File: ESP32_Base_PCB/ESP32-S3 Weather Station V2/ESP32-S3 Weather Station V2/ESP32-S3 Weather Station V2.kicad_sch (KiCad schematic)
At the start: 40 parts, among them J1 USB_C_Receptacle_USB2.0_16P, J10 A3 of ADC, J11 External Power, J2 Rain Guage, J3 GPIO, J4 Wind Speed/DIR, J5 BME680, J6 Light Density, J7 Soil Mouisture, J8 I2C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

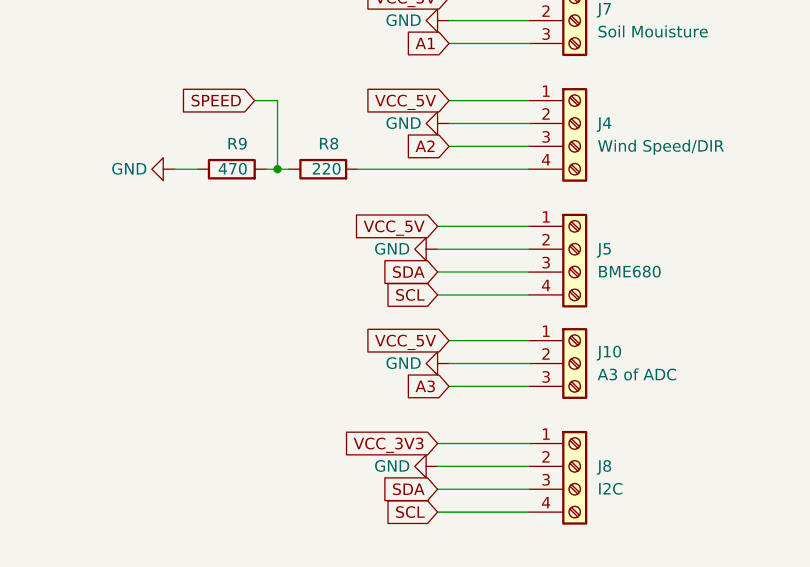
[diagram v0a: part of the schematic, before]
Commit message: Created GRBR File
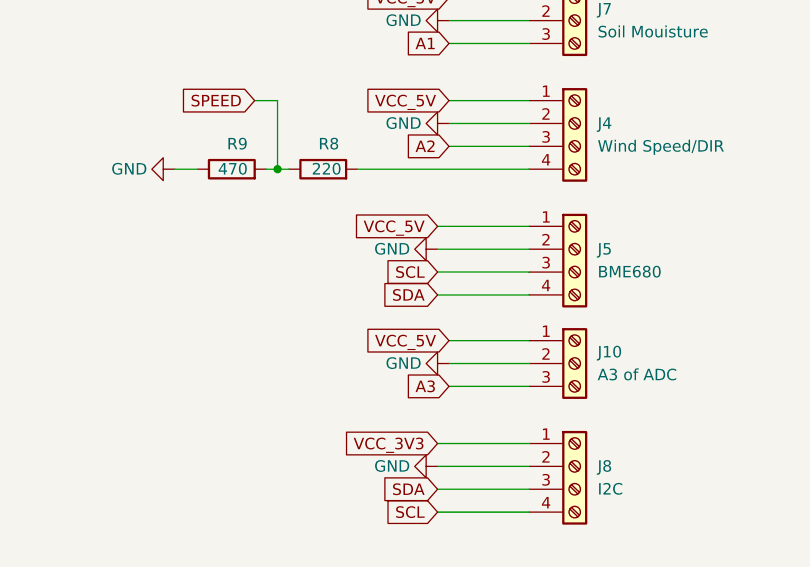
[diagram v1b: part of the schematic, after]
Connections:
- net SCL: now also J5.3 (Pin_3); no longer J5.4 (Pin_4)
- net SDA: now also J5.4 (Pin_4); no longer J5.3 (Pin_3)

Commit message: now?
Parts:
- C1, C2, C4, C9: Manufacturer_Part_Number (none) -> 0805W106K500CC
- C10, C3, C5, C6, C7: Manufacturer_Part_Number (none) -> 0805B104K101CC
- C8: Manufacturer_Part_Number (none) -> 0805B105K250DC
- D1: Manufacturer_Part_Number (none) -> 1N5819
- D2, D3, D4: value LESD5D5.0CT1G -> ESD5Z12V; Manufacturer_Name (none) -> ESD5Z12V; Manufacturer_Part_Number (none) -> ESD5Z12V
- D5: Manufacturer_Part_Number (none) -> 0603GBD0790S01
- D6: value SK6812 -> Adafruit SK6812; Manufacturer_Part_Number (none) -> 1655
- J1: Manufacturer_Part_Number (none) -> USB4105-GF-A
- J10, J11, J7: Manufacturer_Part_Number (none) -> 282837-3
- J2, J6: Manufacturer_Part_Number (none) -> 282837-2
- J3, J4, J5, J8: Manufacturer_Part_Number (none) -> 282837-4
- R1, R2: Manufacturer_Part_Number (none) -> RC0603FR-075K1L
- R3: Manufacturer_Part_Number (none) -> RC0603FR-0775RL
- R4, R5, R6: Manufacturer_Part_Number (none) -> RC0603FR-0710KL
- R7: footprint Resistor_SMD:R_0603_1608Metric_Pad0.98x0.95mm_HandSolder -> Resistor_THT:R_Axial_DIN0207_L6.3mm_D2.5mm_P10.16mm_Horizontal
- R8: Manufacturer_Part_Number (none) -> RMCF0603JT220R
- R9: Manufacturer_Part_Number (none) -> RL0603FR-070R47L
- SW1, SW2: value PTS810_SJM_250_SMTR_LFS -> PTS 647 SN50 SMTR2 LFS; footprint PTS815_SJG_250_SMTR_LFS:PTS815SJG250SMTRLFS -> PTS_647_SN50_SMTR2_LFS:SW_PTS_647_SN50_SMTR2_LFS; Manufacturer_Part_Number (none) -> PTS 647 SN50 SMTR2 LFS
- U1: Manufacturer_Part_Number (none) -> AMS1117-3.3
- U2: Manufacturer_Part_Number (none) -> ESP32-S3-WROOM-2-N32R8V
- U3: Manufacturer_Part_Number (none) -> ADS1015IDGS
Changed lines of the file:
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@@
 			)
 		)
-		(property "Manufacturer_Part_Number" ""
+		(property "Manufacturer_Part_Number" "1N5819"
 			(at 66.04 55.88 0)
 			(effects
@@
 			)
 		)
-		(property "Manufacturer_Part_Number" ""
+		(property "Manufacturer_Part_Number" "0805B104K101CC"
 			(at 420.37 66.04 0)
 			(effects
@@
 			)
 		)
-		(property "Manufacturer_Part_Number" ""
+		(property "Manufacturer_Part_Number" "0805W106K500CC"
 			(at 90.17 55.88 0)
 			(effects
@@
 			)
 		)
-		(property "Manufacturer_Part_Number" ""
+		(property "Manufacturer_Part_Number" "282837-4"
 			(at 360.68 252.73 0)
 			(effects
@@
 			)
 		)
-		(property "Manufacturer_Part_Number" ""
+		(property "Manufacturer_Part_Number" "0603GBD0790S01"
 			(at 190.5 54.61 0)
 			(effects
@@
 			)
 		)
-		(property "Manufacturer_Part_Number" ""
+		(property "Manufacturer_Part_Number" "0805W106K500CC"
 			(at 127 55.88 0)
 			(effects
@@
 			)
 		)
-		(property "Manufacturer_Part_Number" ""
+		(property "Manufacturer_Part_Number" "282837-3"
 			(at 360.68 176.53 0)
 			(effects
@@
 			)
 		)
-		(property "Value" "LESD5D5.0CT1G"
+		(property "Value" "ESD5Z12V"
 			(at 72.898 76.962 0)
 			(effects
@@
 			)
 		)
-		(property "Manufacturer_Name" ""
+		(property "Manufacturer_Name" "ESD5Z12V"
 			(at 69.85 82.55 0)
 			(effects
@@
 			)
 		)
-		(property "Manufacturer_Part_Number" ""
+		(property "Manufacturer_Part_Number" "ESD5Z12V"
 			(at 69.85 82.55 0)
 			(effects
@@
 			)
 		)
-		(property "Value" "PTS810_SJM_250_SMTR_LFS"
+		(property "Value" "PTS 647 SN50 SMTR2 LFS"
 			(at 407.67 52.07 0)
 			(effects
@@
 			)
 		)
-		(property "Footprint" "PTS815_SJG_250_SMTR_LFS:PTS815SJG250SMTRLFS"
+		(property "Footprint" "PTS_647_SN50_SMTR2_LFS:SW_PTS_647_SN50_SMTR2_LFS"
 			(at 407.67 52.07 0)
 			(effects
@@
 			)
 		)
-		(property "Manufacturer_Part_Number" ""
+		(property "Manufacturer_Part_Number" "PTS 647 SN50 SMTR2 LFS"
 			(at 407.67 59.69 0)
 			(effects
@@
 			)
 		)
-		(property "Manufacturer_Part_Number" ""
+		(property "Manufacturer_Part_Number" "0805B105K250DC"
 			(at 52.07 165.1 0)
 			(effects
@@
 			)
 		)
-		(property "Value" "PTS810_SJM_250_SMTR_LFS"
+		(property "Value" "PTS 647 SN50 SMTR2 LFS"
 			(at 350.52 52.07 0)
 			(effects
@@
 			)
 		)
-		(property "Footprint" "PTS815_SJG_250_SMTR_LFS:PTS815SJG250SMTRLFS"
+		(property "Footprint" "PTS_647_SN50_SMTR2_LFS:SW_PTS_647_SN50_SMTR2_LFS"
 			(at 350.52 52.07 0)
 			(effects
@@
 			)
 		)
-		(property "Manufacturer_Part_Number" ""
+		(property "Manufacturer_Part_Number" "PTS 647 SN50 SMTR2 LFS"
 			(at 350.52 59.69 0)
 			(effects
@@
 			)
 		)
-		(property "Value" "LESD5D5.0CT1G"
+		(property "Value" "ESD5Z12V"
 			(at 77.724 76.708 0)
 			(effects
@@
 			)
 		)
-		(property "Manufacturer_Name" ""
+		(property "Manufacturer_Name" "ESD5Z12V"
 			(at 74.93 82.55 0)
 			(effects
@@
 			)
 		)
-		(property "Manufacturer_Part_Number" ""
+		(property "Manufacturer_Part_Number" "ESD5Z12V"
 			(at 74.93 82.55 0)
 			(effects
@@
 			)
 		)
-		(property "Manufacturer_Part_Number" ""
+		(property "Manufacturer_Part_Number" "282837-3"
 			(at 360.68 214.63 0)
 			(effects
@@
 			)
 		)
-		(property "Manufacturer_Part_Number" ""
+		(property "Manufacturer_Part_Number" "282837-4"
 			(at 360.68 201.93 0)
 			(effects
@@
 			)
 		)
-		(property "Manufacturer_Part_Number" ""
+		(property "Manufacturer_Part_Number" "RMCF0603JT220R"
 			(at 332.74 193.04 0)
 			(effects
@@
 			)
 		)
-		(property "Manufacturer_Part_Number" ""
+		(property "Manufacturer_Part_Number" "RC0603FR-0710KL"
 			(at 370.84 54.61 0)
 			(effects
@@
 			)
 		)
-		(property "Footprint" "Resistor_SMD:R_0603_1608Metric_Pad0.98x0.95mm_HandSolder"
+		(property "Footprint" "Resistor_THT:R_Axial_DIN0207_L6.3mm_D2.5mm_P10.16mm_Horizontal"
 			(at 337.058 154.94 90)
 			(effects
@@
 			)
 		)
-		(property "Manufacturer_Part_Number" ""
+		(property "Manufacturer_Part_Number" "RC0603FR-075K1L"
 			(at 66.04 66.04 0)
 			(effects
@@
 			)
 		)
-		(property "Manufacturer_Part_Number" ""
+		(property "Manufacturer_Part_Number" "RC0603FR-0710KL"
 			(at 52.07 152.4 0)
 			(effects
@@
 			)
 		)
-		(property "Manufacturer_Part_Number" ""
+		(property "Manufacturer_Part_Number" "ESP32-S3-WROOM-2-N32R8V"
 			(at 76.2 199.39 0)
 			(effects
@@
 			)
 		)
-		(property "Manufacturer_Part_Number" ""
+		(property "Manufacturer_Part_Number" "RC0603FR-0775RL"
 			(at 182.88 48.26 0)
 			(effects
@@
 			)
 		)
-		(property "Manufacturer_Part_Number" ""
+		(property "Manufacturer_Part_Number" "282837-2"
 			(at 360.68 165.1 0)
 			(effects
@@
 			)
 		)
-		(property "Manufacturer_Part_Number" ""
+		(property "Manufacturer_Part_Number" "282837-4"
 			(at 360.68 226.06 0)
 			(effects
@@
 			)
 		)
-		(property "Manufacturer_Part_Number" ""
+		(property "Manufacturer_Part_Number" "RC0603FR-0710KL"
 			(at 427.99 54.61 0)
 			(effects
@@
 			)
 		)
-		(property "Manufacturer_Part_Number" ""
+		(property "Manufacturer_Part_Number" "0805B104K101CC"
 			(at 66.04 137.16 0)
 			(effects
@@
 			)
 		)
-		(property "Manufacturer_Part_Number" ""
+		(property "Manufacturer_Part_Number" "RL0603FR-070R47L"
 			(at 322.58 193.04 0)
 			(effects
@@
 			)
 		)
-		(property "Manufacturer_Part_Number" ""
+		(property "Manufacturer_Part_Number" "0805W106K500CC"
 			(at 60.96 137.16 0)
 			(effects
@@
 			)
 		)
-		(property "Manufacturer_Part_Number" ""
+		(property "Manufacturer_Part_Number" "0805W106K500CC"
 			(at 170.18 54.61 0)
 			(effects
@@
 			)
 		)
-		(property "Manufacturer_Part_Number" ""
+		(property "Manufacturer_Part_Number" "0805B104K101CC"
 			(at 132.08 55.88 0)
 			(effects
@@
 			)
 		)
-		(property "Manufacturer_Part_Number" ""
+		(property "Manufacturer_Part_Number" "282837-3"
 			(at 360.68 265.43 0)
 			(effects
@@
 			)
 		)
-		(property "Manufacturer_Part_Number" ""
+		(property "Manufacturer_Part_Number" "0805B104K101CC"
 			(at 363.22 66.04 0)
 			(effects
@@
 			)
 		)
-		(property "Manufacturer_Part_Number" ""
+		(property "Manufacturer_Part_Number" "  USB4105-GF-A"
 			(at 40.64 71.12 0)
 			(effects
@@
 			)
 		)
-		(property "Manufacturer_Part_Number" ""
+		(property "Manufacturer_Part_Number" "ADS1015IDGS"
 			(at 191.77 170.18 0)
 			(effects
@@
 			)
 		)
-		(property "Manufacturer_Part_Number" ""
+		(property "Manufacturer_Part_Number" "0805B104K101CC"
 			(at 175.26 54.61 0)
 			(effects
@@
 			)
 		)
-		(property "Value" "LESD5D5.0CT1G"
+		(property "Value" "ESD5Z12V"
 			(at 58.928 43.18 0)
 			(effects
@@
 			)
 		)
-		(property "Manufacturer_Name" ""
+		(property "Manufacturer_Name" "ESD5Z12V"
 			(at 64.77 45.72 0)
 			(effects
@@
 			)
 		)
-		(property "Manufacturer_Part_Number" ""
+		(property "Manufacturer_Part_Number" "ESD5Z12V"
 			(at 64.77 45.72 0)
 			(effects
@@
 			)
 		)
-		(property "Manufacturer_Part_Number" ""
+		(property "Manufacturer_Part_Number" "RC0603FR-075K1L"
 			(at 66.04 60.96 0)
 			(effects
@@
 			)
 		)
-		(property "Manufacturer_Part_Number" ""
+		(property "Manufacturer_Part_Number" "AMS1117-3.3"
 			(at 153.67 48.26 0)
 			(effects
@@
 			)
 		)
-		(property "Value" "SK6812"
+		(property "Value" " Adafruit SK6812"
 			(at 283.718 59.69 0)
 			(effects
@@
 			)
 		)
-		(property "Manufacturer_Part_Number" ""
+		(property "Manufacturer_Part_Number" "1655"
 			(at 274.32 63.5 0)
 			(effects
@@
 			)
 		)
-		(property "Manufacturer_Part_Number" ""
+		(property "Manufacturer_Part_Number" "282837-4"
 			(at 360.68 187.96 0)
 			(effects
@@
 			)
 		)
-		(property "Manufacturer_Part_Number" ""
+		(property "Manufacturer_Part_Number" "282837-2"
 			(at 360.68 156.21 0)
 			(effects
